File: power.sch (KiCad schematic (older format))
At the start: 28 parts, among them IC1 OSD335x, J19 VDD_3V3AUX, J3 GS2, U1 AP2112K-3.3TRG1, U2 AP2112K-1.8TRG1, U3 TL1963A-33DCQR, U4 24LC32AT-I

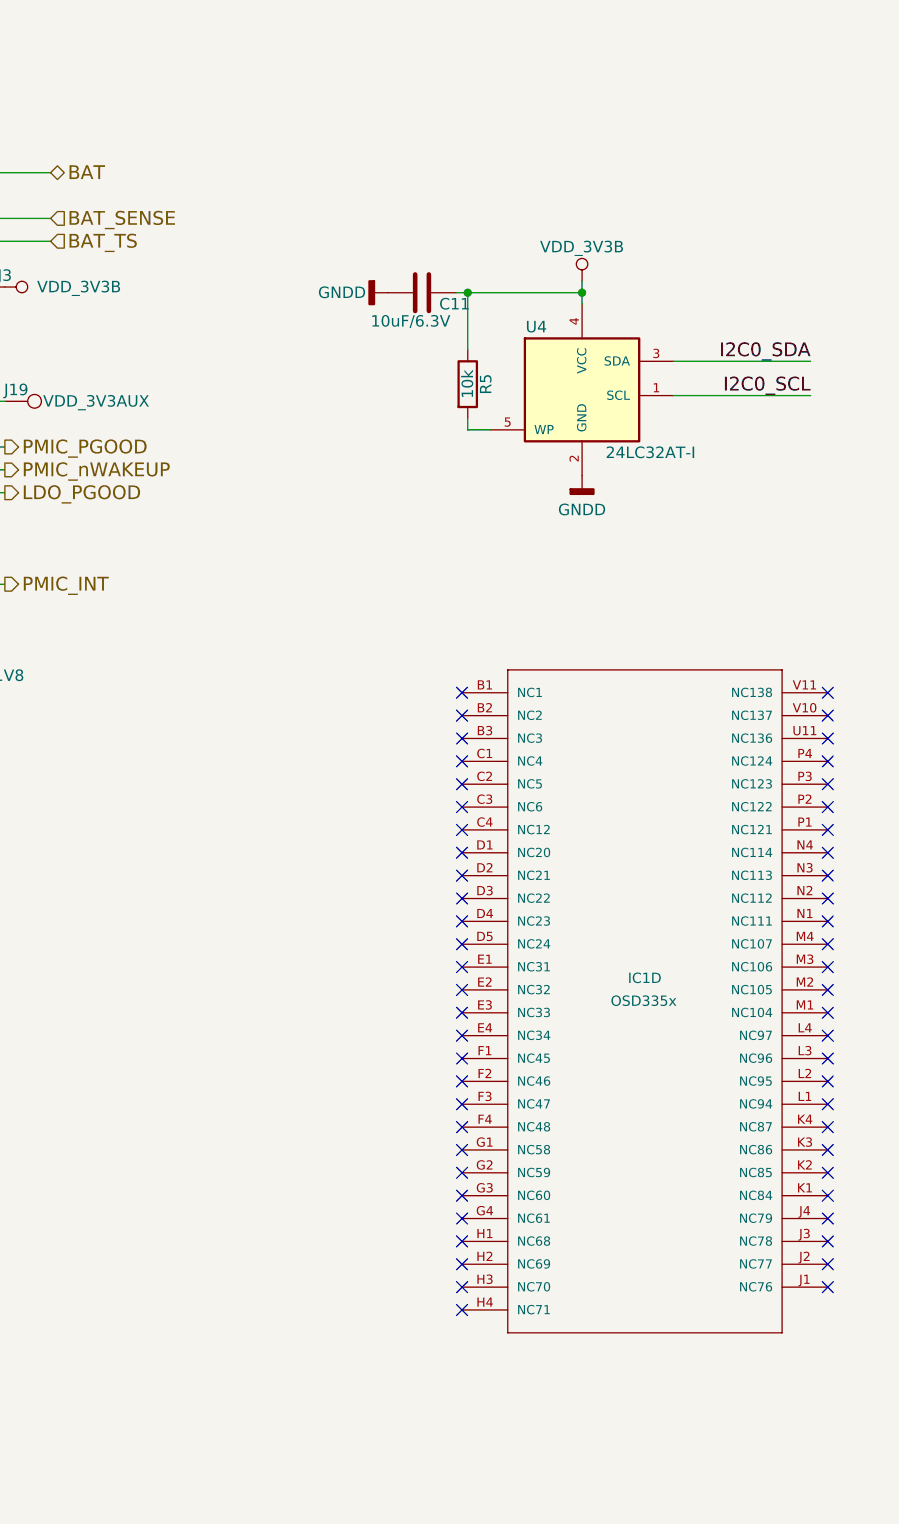
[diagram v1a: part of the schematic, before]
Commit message: add clamping protection for 3v3a and 3v3b
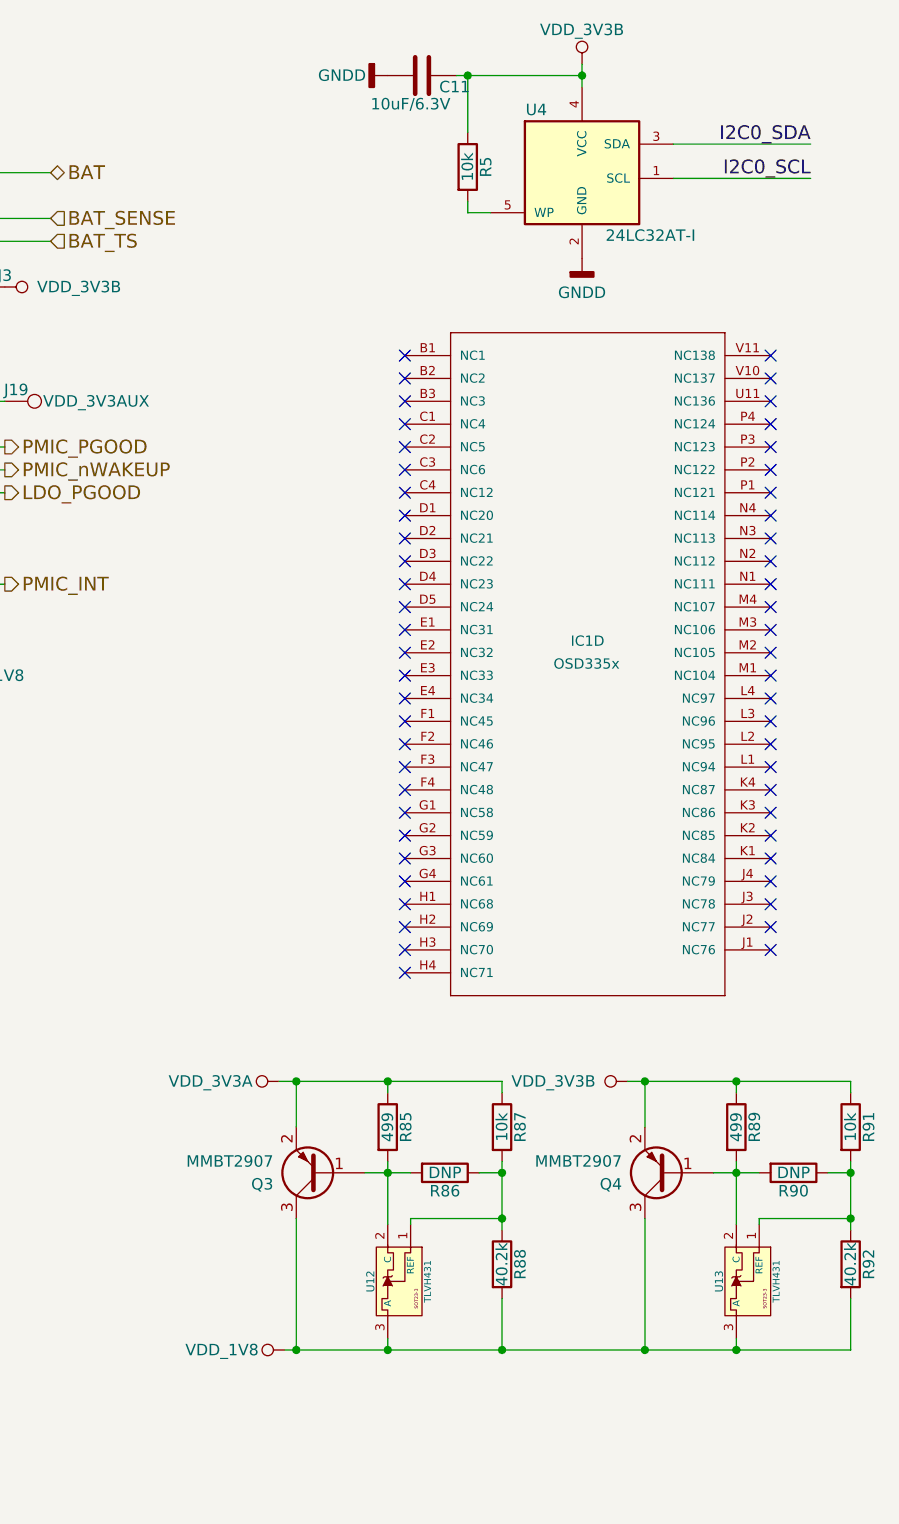
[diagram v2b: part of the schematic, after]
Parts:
- added Q3, Q4: MMBT2907, TO_SOT_Packages_SMD:SOT-23, symbol Q_PNP_BEC
- added R85, R89: 499, Resistors_SMD:R_0402, symbol R
- added R86, R90: DNP, Resistors_SMD:R_0402, symbol R
- added R87, R91: 10k, Resistors_SMD:R_0402, symbol R
- added R88, R92: 40.2k, Resistors_SMD:R_0402, symbol R
- added U12, U13: TLVH431, TO_SOT_Packages_SMD:SOT-23, symbol TLV431
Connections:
- net VDD_1V8: now also Q3.3 (C), Q4.3 (C), R88.2, R92.2, U12.3 (A), U13.3 (A)
- net VDD_3V3A: now also Q3.2 (E), R85.1, R87.1
- net VDD_3V3B: now also Q4.2 (E), R89.1, R91.1
- new net: Q3.1 (B), R85.2, R86.2, U12.2 (C)
- new net: R86.1, R87.2, R88.1, U12.1 (REF)
- new net: Q4.1 (B), R89.2, R90.2, U13.2 (C)
- new net: R90.1, R91.2, R92.1, U13.1 (REF)
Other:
- moved on the sheet: C11, IC1D, R5, U4

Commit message: sch updated
Signed-off-by: Pablo Ridolfi <pabloridolfi@outlook.com>
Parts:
- added D7: LTST-C191TBKT, LEDs:LED_0603, symbol LED
- added R93: 4.75k, Resistors_SMD:R_0402, symbol R
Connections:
- net GNDD: now also D7.1 (K)
- net at IC1.Y11 (VDD_3V3AUX), J19.1: now also R93.1
- new net: D7.2 (A), R93.2
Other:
- moved on the sheet: J19
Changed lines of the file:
@@
 LIBS:osd335x
 LIBS:mateboard-cache
-EELAYER 25 0
+EELAYER 26 0
 EELAYER END
 $Descr A4 11693 8268
 encoding utf-8
 Sheet 2 6
-Title ""
-Date ""
-Rev ""
-Comp ""
-Comment1 ""
-Comment2 ""
-Comment3 ""
+Title "Mateboard"
+Date "2017-06-21"
+Rev "1.00"
+Comp "DPLab@UTN-FRBA"
+Comment1 "Director: Alejandro Furfaro"
+Comment2 "Revisor: Nicolás Dassieu Blanchet"
+Comment3 "Autor: Pablo Ridolfi"
 Comment4 ""
 $EndDescr
@@
 	3650 2825 4050 2825
 Wire Wire Line
-	7100 2225 6450 2225
+	8100 2225 6450 2225
 Connection ~ 6550 1725
 Wire Wire Line
@@
 L TEST_1P J19
 U 1 1 5906996C
-P 7100 2225
-F 0 "J19" V 7050 2275 50  0000 C CNN
-F 1 "VDD_3V3AUX" V 7100 2625 50  0000 C CNN
-F 2 "Measurement_Points:Measurement_Point_Round-SMD-Pad_Small" H 7300 2225 50  0001 C CNN
-F 3 "" H 7300 2225 50  0001 C CNN
-	1    7100 2225
+P 8100 2225
+F 0 "J19" V 8050 2275 50  0000 C CNN
+F 1 "VDD_3V3AUX" V 8100 2625 50  0000 C CNN
+F 2 "Measurement_Points:Measurement_Point_Round-SMD-Pad_Small" H 8300 2225 50  0001 C CNN
+F 3 "" H 8300 2225 50  0001 C CNN
+	1    8100 2225
 	0    1    1    0
 $EndComp
@@
 	-1   0    0    1
 $EndComp
+$Comp
+L LED D7
+U 1 1 594BBB6F
+P 8000 2700
+F 0 "D7" V 8050 2575 50  0000 C CNN
+F 1 "LTST-C191TBKT" V 7975 2325 50  0000 C CNN
+F 2 "LEDs:LED_0603" H 8000 2700 50  0001 C CNN
+F 3 "" H 8000 2700 50  0000 C CNN
+	1    8000 2700
+	0    -1   -1   0
+$EndComp
+$Comp
+L R R93
+U 1 1 594BBB76
+P 8000 2400
+F 0 "R93" H 8125 2425 50  0000 C CNN
+F 1 "4.75k" H 8175 2350 50  0000 C CNN
+F 2 "Resistors_SMD:R_0402" V 7930 2400 50  0001 C CNN
+F 3 "" H 8000 2400 50  0000 C CNN
+	1    8000 2400
+	1    0    0    -1
+$EndComp
+$Comp
+L GNDD #PWR073
+U 1 1 594BC0DD
+P 8000 2850
+F 0 "#PWR073" H 8000 2600 50  0001 C CNN
+F 1 "GNDD" H 8000 2700 50  0000 C CNN
+F 2 "" H 8000 2850 50  0000 C CNN
+F 3 "" H 8000 2850 50  0000 C CNN
+	1    8000 2850
+	1    0    0    -1
+$EndComp
+Wire Wire Line
+	8000 2250 8000 2225
+Connection ~ 8000 2225
 $EndSCHEMATC

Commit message: sch updated
Signed-off-by: Pablo Ridolfi <pabloridolfi@outlook.com>
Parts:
- removed unit 3 of IC1
- added unit 3 of IC1
- IC1: symbol OSD335x-RESCUE-mateboard -> OSD335x
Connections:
- net BAT: now also IC1.Y2 (BAT_1), IC1.Y3 (BAT_2)
- net BAT_SENSE: now also IC1.Y1 (BATT_VOLT)
- net BAT_TS: now also IC1.W1 (BAT_TEMP)
- net I2C0_SCL: now also IC1.C16 (I2C0_SCL), IC1.C20 (PMIC_I2C_SCL)
- net I2C0_SDA: now also IC1.C17 (I2C0_SDA), IC1.C19 (PMIC_I2C_SDA)
- net LDO_PGOOD: now also IC1.B20 (PMIC_LDO_PGOOD)
- net PMIC_INT: now also IC1.B19 (PMIC_INTN)
- net PMIC_PGOOD: now also IC1.A20 (PMIC_PGOOD)
- net PMIC_nWAKEUP: now also IC1.A19 (PMIC_WAKEUPN)
- net PWR_BUT: now also IC1.D20 (PWR_BUT)
- net SYS_5V: now also IC1.W4 (SYS_5V_1), IC1.Y4 (SYS_5V_2)
- net USB_DC: now also IC1.Y8 (VIN_USB_0), IC1.Y9 (VIN_USB_1)
- net VDD_1V8: now also IC1.N16 (VDD_1V8_0), IC1.R16 (VDD_1V8_1)
- net VDD_5V: now also IC1.Y5 (VIN_5V_0), IC1.Y6 (VIN_5V_1)
- net at J3.2 (G2): now also IC1.U20 (VDD_3V3B_0), IC1.V20 (VDD_3V3B_1)
- net VDD_3V3AUX: now reaches J19.1, R93.1
- net VDD_3V3AUX: now also IC1.Y11 (VDD_3V3AUX)
- new net: IC1.C6 (PMIC_POWER_EN), IC1.D19 (PWR_EN)
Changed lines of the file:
@@
 Sheet 2 6
 Title "Mateboard"
-Date "2017-06-21"
+Date "2017-06-23"
 Rev "1.00"
 Comp "DPLab@UTN-FRBA"
@@
 $EndComp
 $Comp
-L OSD335x-RESCUE-mateboard IC1
-U 3 1 58DB60E7
-P 5250 3025
-AR Path="/58DB60E7" Ref="IC1"  Part="3"
-AR Path="/589A190D/58DB60E7" Ref="IC1"  Part="3"
-F 0 "IC1" H 5175 3050 45  0000 L BNN
-F 1 "OSD335x" H 5100 2950 45  0000 L BNN
-F 2 "footprints:OSD3358-BAS-BGA400" H 5280 3175 20  0001 C CNN
-F 3 "" H 5250 3025 60  0001 C CNN
-	3    5250 3025
-	1    0    0    -1
-$EndComp
-$Comp
 L VDD_3V3B #PWR050
 U 1 1 58DBD053
@@
 NoConn ~ 6450 5125
 $Comp
-L OSD335x-RESCUE-mateboard IC1
+L OSD335x IC1
 U 4 1 58DC3495
 P 9650 3325
@@
 	8000 2250 8000 2225
 Connection ~ 8000 2225
+Text Label 7350 2225 0    60   ~ 0
+VDD_3V3AUX
+$Comp
+L OSD335x IC1
+U 3 1 594B7B3B
+P 5250 3025
+AR Path="/594B7B3B" Ref="IC1"  Part="3"
+AR Path="/589A190D/594B7B3B" Ref="IC1"  Part="3"
+F 0 "IC1" H 5250 5379 45  0000 C CNN
+F 1 "OSD335x" H 5250 5295 45  0000 C CNN
+F 2 "GHI-SoMs-Processors_OSD3358" H 5280 3175 20  0001 C CNN
+F 3 "" H 5250 3025 60  0001 C CNN
+	3    5250 3025
+	1    0    0    -1
+$EndComp
 $EndSCHEMATC

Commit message: footprints updated, add power led
Signed-off-by: Pablo Ridolfi <pabloridolfi@outlook.com>
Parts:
- IC1: footprint GHI-SoMs-Processors_OSD3358 -> footprints:OSD3358-BAS-BGA400
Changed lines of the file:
@@
 F 0 "IC1" H 5250 5379 45  0000 C CNN
 F 1 "OSD335x" H 5250 5295 45  0000 C CNN
-F 2 "GHI-SoMs-Processors_OSD3358" H 5280 3175 20  0001 C CNN
+F 2 "footprints:OSD3358-BAS-BGA400" H 5280 3175 20  0001 C CNN
 F 3 "" H 5250 3025 60  0001 C CNN
 	3    5250 3025

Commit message: gerbers updated, bom using kicost
Signed-off-by: Pablo Ridolfi <pabloridolfi@outlook.com>
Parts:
- C1: manf# (none) -> GCM188R70J225KE22D
- C10: manf# (none) -> C1608X5R0J106M080AB
- C4: manf# (none) -> GRM155R60J104KA01D
- D1: manf# (none) -> STPS140A
- D4: manf# (none) -> BAT54C
- D7: manf# (none) -> LTST-C191TBKT-5A
- IC1: manf# (none) -> OSD3358-512M-BAS
- L1: manf# (none) -> BLM21AG221SN1D
- Q3: manf# (none) -> MMBT2907ALT1G
- R1: manf# (none) -> RC0402FR-071ML
- R2: manf# (none) -> RC0402FR-071KL
- R3: manf# (none) -> RC0402FR-071K5L
- R85: manf# (none) -> RC0402FR-07499RL
- R88: manf# (none) -> RC0402FR-0740K2L
- R93: manf# (none) -> RC0402FR-074K75L
- U1: manf# (none) -> AP2112K-3.3TRG1
- U12: manf# (none) -> TLVH431IDBZR
- U2: manf# (none) -> AP2112K-1.8TRG1
- U3: manf# (none) -> TL1963A-33DCQR
- U4: manf# (none) -> 24LC32AT-I/OT
